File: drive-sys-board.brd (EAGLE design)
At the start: 109.9 x 50.2 mm, 31 parts, among them J2 APP_2POS_CONFIG12V_HORIZ, U1 OKI-78SR-5/1.5-W36HC, U2 MAX232, U3 MAX232, U4 MAX232

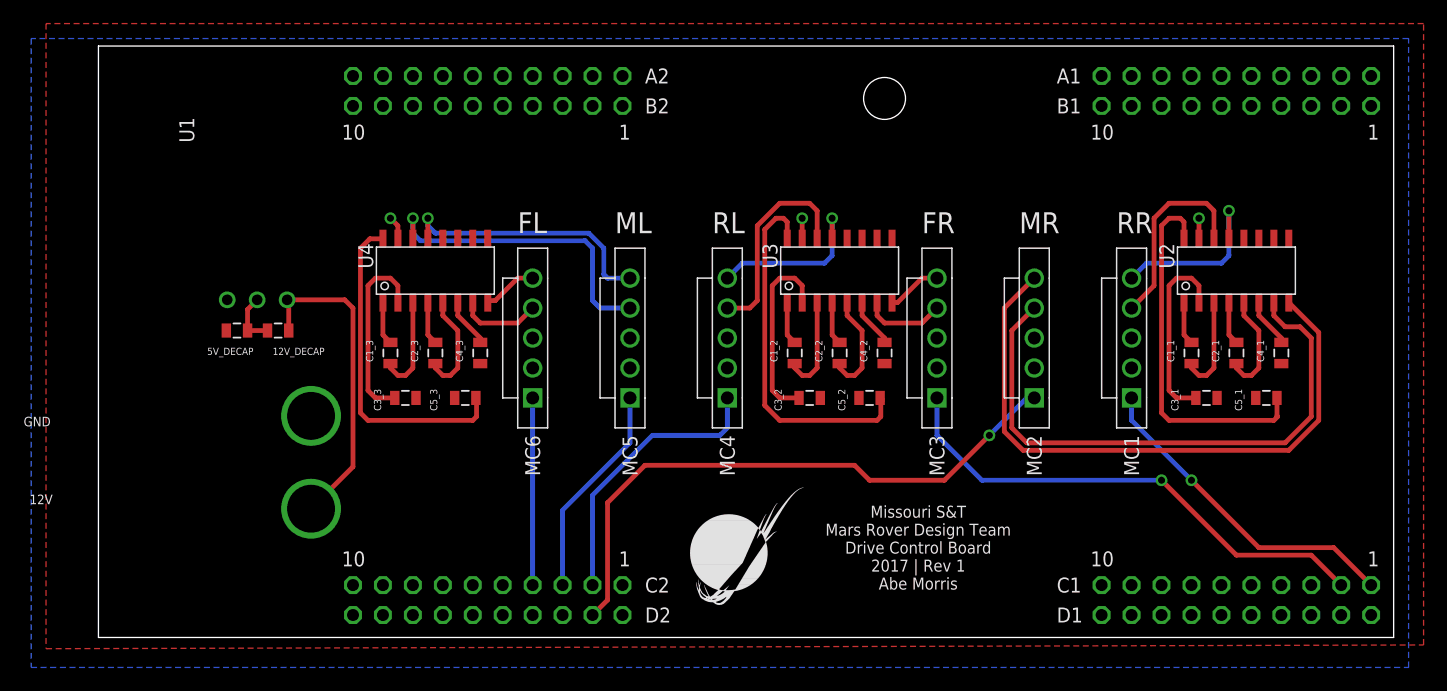
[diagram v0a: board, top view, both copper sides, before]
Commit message: Fixed RS232 chip capacitors
Several capacitors were going to Vcc when they should have been going to
Gnd
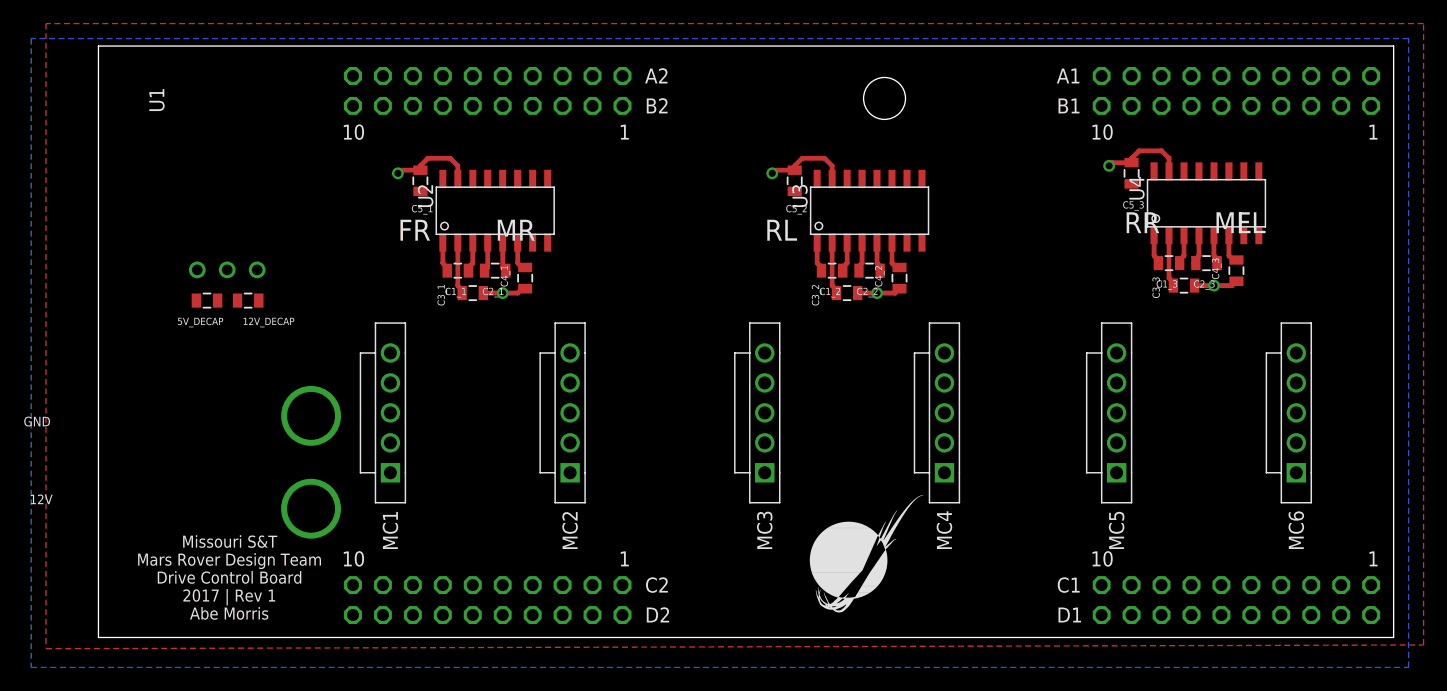
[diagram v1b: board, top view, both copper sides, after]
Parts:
- moved C5_1 74.1 mm to (27.3, 38.7), turned to 270 degrees
- moved C3_3 66.7 mm to (92.1, 29.8)
- moved C1_3 66.5 mm to (90.8, 31.8), turned to 180 degrees
- moved C2_3 65.8 mm to (94.0, 31.8), turned to 180 degrees
- moved U4 65.7 mm to (94.0, 36.8)
- moved MC6 65.1 mm to (101.6, 19.1)
- moved C4_3 64.5 mm to (96.5, 31.1)
- moved C4_1 64.4 mm to (36.2, 30.5)
- moved C2_1 63.3 mm to (33.7, 31.1), turned to 180 degrees
- moved MC1 63.2 mm to (24.8, 19.1)
- moved U2 63.1 mm to (33.7, 36.2)
- moved C3_1 62.9 mm to (31.8, 29.2)
- moved C1_1 62.6 mm to (30.5, 31.1), turned to 180 degrees
- moved C5_3 59.6 mm to (87.6, 39.4), turned to 270 degrees
- moved MC5 41.8 mm to (86.4, 19.1)
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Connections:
- removed net N$10: C5_1.1, U2.16
- removed net N$17: C5_2.1, U3.16
- removed net N$24: C5_3.1, U4.16
- net +5V: now also U2.16, U3.16, U4.16; no longer C3_1.1, C3_2.1, C3_3.1, C4_1.1, C4_2.1, C4_3.1
- net GND: now also C3_1.1, C3_2.1, C3_3.1, C4_1.1, C4_2.1, C4_3.1, C5_1.1, C5_2.1, C5_3.1
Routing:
- net N$34: track 53.5 -> 0.00 mm
- net PWM_2: track 51.0 -> 0.00 mm, vias 1 -> 0
- net N$35: track 49.5 -> 0.00 mm
- net PWM_3: track 42.7 -> 0.00 mm, vias 1 -> 0
- net N$10: track 31.4 -> 0.00 mm
- net N$17: track 31.1 -> 0.00 mm
- net N$24: track 28.1 -> 0.00 mm
- net PWM_1: track 28.0 -> 0.00 mm, vias 1 -> 0
- net N$5: track 27.0 -> 0.00 mm
- net N$26: track 26.7 -> 0.00 mm, vias 1 -> 0
- net PWM_4: track 24.0 -> 0.00 mm
- net N$29: track 22.7 -> 0.00 mm, vias 1 -> 0
- net GND: track 10.1 -> 32.7 mm, vias 3 -> 6
- net PWM_5: track 18.2 -> 0.00 mm
- net N$32: track 17.7 -> 0.00 mm
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
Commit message: Began routing traces
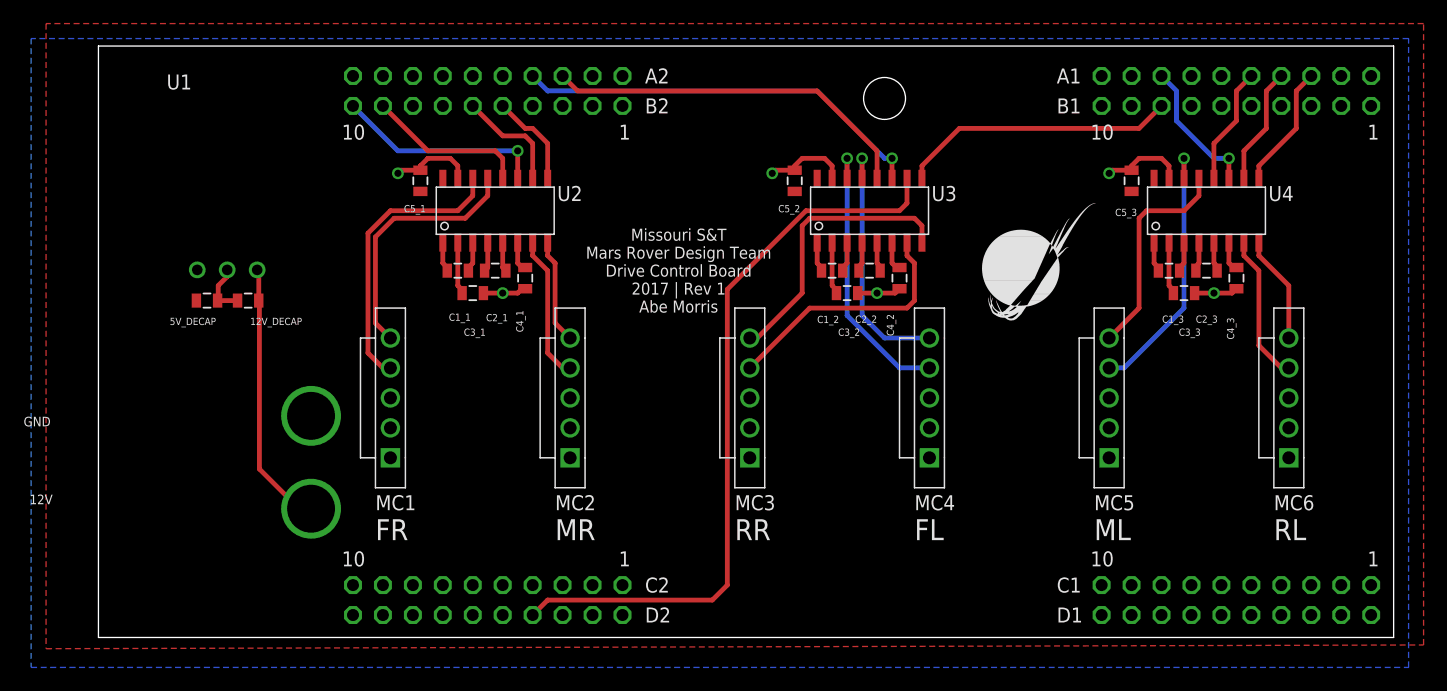
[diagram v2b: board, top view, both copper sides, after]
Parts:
- moved U$2 28.8 mm to (74.9, 26.0)
- moved MC3 1.80 mm to (55.2, 20.3)
- moved MC4 1.80 mm to (70.5, 20.3)
- moved MC5 1.42 mm to (85.7, 20.3)
- moved MC6 1.42 mm to (101.0, 20.3)
- moved MC1 1.27 mm to (24.8, 20.3)
- moved MC2 1.27 mm to (40.0, 20.3)
- moved C1_3 0.64 mm to (90.8, 31.1)
- moved C2_3 0.64 mm to (94.0, 31.1)
- moved C3_3 0.63 mm to (92.1, 29.2)
- moved C4_3 0.63 mm to (96.5, 30.5)
- moved C5_3 0.63 mm to (87.6, 38.7)
- moved U4 0.63 mm to (94.0, 36.2)
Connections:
- new net PWM1: U$1.PF1
- new net PWM2: U$1.PM7
- new net PWM3: U$1.PF2
- new net PWM4: U$1.PK4
- new net PWM5: U$1.PK5
- new net PWM6: U$1.PM0
- net PWM_1: no longer U$1.PF1
- net PWM_2: no longer U$1.PM7
- net PWM_3: no longer U$1.PF2
- net PWM_4: no longer U$1.PK4
- net PWM_5: no longer U$1.PK5
- net PWM_6: no longer U$1.PM0
- net RX_1: now also U$1.PA4; no longer U$1.PA6
- net RX_2: now also U$1.PK0; no longer U$1.PA4
- net RX_3: now also U$1.PP0; no longer U$1.PK0
- net RX_4: now also U$1.PA6; no longer U$1.PC6
- net RX_5: now also U$1.PC6; no longer U$1.PP0
- net TX_1: now also U$1.PA5; no longer U$1.PA7
- net TX_2: now also U$1.PK1; no longer U$1.PA5
- net TX_3: now also U$1.PP1; no longer U$1.PK1
- net TX_4: now also U$1.PA7; no longer U$1.PC7
- net TX_5: now also U$1.PC7; no longer U$1.PP1
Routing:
- net TX_4: track 0.00 -> 63.0 mm
- net TX_3: track 0.00 -> 35.1 mm, vias 0 -> 1
- net RX_3: track 0.00 -> 31.7 mm
- net N$36: track 0.00 -> 24.2 mm
- net N$32: track 0.00 -> 23.9 mm, vias 0 -> 1
- net N$30: track 0.00 -> 23.9 mm
- net RX_4: track 0.00 -> 23.5 mm
- net N$26: track 0.00 -> 22.9 mm, vias 0 -> 1
- net N$5: track 0.00 -> 22.7 mm
- net N$33: track 0.00 -> 21.6 mm, vias 0 -> 1
- net N$31: track 0.00 -> 21.5 mm
- net N$37: track 0.00 -> 21.5 mm
- net N$29: track 0.00 -> 18.5 mm
- net TX_1: track 0.00 -> 17.9 mm, vias 0 -> 1
- net RX_1: track 0.00 -> 13.7 mm
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
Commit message: Updated Max232 and Tiva to Eagle libraries commit 9c171e
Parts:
- U$1: value TIVA-C-CONNECTED -> TIVA-1294; device MRDT-2015-General:TIVA-C-CONNECTED -> MRDT-Microcontrollers:TIVA-C-CONNECTED
- U2, U3, U4: value MAX232 -> MAX232D
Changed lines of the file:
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@@
 <?xml version="1.0" encoding="utf-8"?>
 <!DOCTYPE eagle SYSTEM "eagle.dtd">
-<eagle version="7.7.0">
+<eagle version="7.6.0">
 <drawing>
 <settings>
@@
 </autorouter>
 <elements>
-<element name="U$1" library="MRDT-2015-General" package="TIVA-C-CONNECTED" value="TIVA-C-CONNECTED" x="-15.24" y="-6.985" smashed="yes"/>
+<element name="U$1" library="MRDT-Microcontrollers" package="TIVA-C-CONNECTED" value="TIVA-1294" x="-15.24" y="-6.985" smashed="yes"/>
 <element name="U$2" library="MRDT-2015-General" package="MRDT_LOGO" value="" x="74.93" y="26.035"/>
 <element name="U1" library="MRDT-ICs" package="OKI-78SR_HORIZ" value="OKI-78SR-5/1.5-W36HC" x="13.462" y="31.1785" smashed="yes">
@@
 <attribute name="COLOR2" value="BLACK" x="-10.16" y="6.985" size="1.778" layer="27" display="off"/>
 </element>
-<element name="U2" library="MRDT-ICs" package="SOIC16" value="MAX232" x="33.655" y="36.195" smashed="yes">
+<element name="U2" library="MRDT-ICs" package="SOIC16" value="MAX232D" x="33.655" y="36.195" smashed="yes">
 <attribute name="NAME" x="38.91" y="37.02" size="1.27" layer="25" font="vector"/>
 <attribute name="VALUE" x="30.655" y="31.195" size="1.27" layer="27" font="vector"/>
+<attribute name="OPERATING_VOLTAGE" value="5V" x="33.655" y="36.195" size="1.778" layer="27" display="off"/>
 </element>
 <element name="H2" library="MRDT-Hardware" package="#6_SCREW" value="MOUNTING_HOLE#6" x="66.675" y="45.72"/>
@@
 <attribute name="VALUE" x="25.908" y="39.751" size="0.4064" layer="27" rot="R270"/>
 </element>
-<element name="U3" library="MRDT-ICs" package="SOIC16" value="MAX232" x="65.405" y="36.195" smashed="yes">
+<element name="U3" library="MRDT-ICs" package="SOIC16" value="MAX232D" x="65.405" y="36.195" smashed="yes">
 <attribute name="NAME" x="70.66" y="37.02" size="1.27" layer="25" font="vector"/>
 <attribute name="VALUE" x="62.405" y="31.195" size="1.27" layer="27" font="vector"/>
+<attribute name="OPERATING_VOLTAGE" value="5V" x="65.405" y="36.195" size="1.778" layer="27" display="off"/>
 </element>
 <element name="C1_2" library="SparkFun-Capacitors" package="0805" value="1uF" x="62.23" y="31.115" smashed="yes" rot="R180">
@@
 <attribute name="VALUE" x="57.658" y="39.751" size="0.4064" layer="27" rot="R270"/>
 </element>
-<element name="U4" library="MRDT-ICs" package="SOIC16" value="MAX232" x="93.98" y="36.195" smashed="yes">
+<element name="U4" library="MRDT-ICs" package="SOIC16" value="MAX232D" x="93.98" y="36.195" smashed="yes">
 <attribute name="NAME" x="99.235" y="37.02" size="1.27" layer="25" font="vector"/>
 <attribute name="VALUE" x="90.98" y="31.195" size="1.27" layer="27" font="vector"/>
+<attribute name="OPERATING_VOLTAGE" value="5V" x="93.98" y="36.195" size="1.778" layer="27" display="off"/>
 </element>
 <element name="C1_3" library="SparkFun-Capacitors" package="0805" value="1uF" x="90.805" y="31.115" smashed="yes" rot="R180">
@@
 <signals>
 <signal name="GND">
-<contactref element="U$1" pad="GND_1"/>
-<contactref element="U$1" pad="GND_2"/>
-<contactref element="U$1" pad="GND_3"/>
-<contactref element="U$1" pad="GND_4"/>
+<contactref element="U$1" pad="GND_1" route="any" routetag="G$1.GND"/>
+<contactref element="U$1" pad="GND_2" route="any" routetag="G$1.GND"/>
+<contactref element="U$1" pad="GND_3" route="any" routetag="G$1.GND"/>
+<contactref element="U$1" pad="GND_4" route="any" routetag="G$1.GND"/>
 <polygon width="0.4064" layer="16">
 <vertex x="-5.715" y="50.8"/>
@@
 <vertex x="112.395" y="52.07"/>
 </polygon>
-<contactref element="U$1" pad="+5V_1"/>
-<contactref element="U$1" pad="+5V_2"/>
+<contactref element="U$1" pad="+5V_1" route="any" routetag="G$1.+5V"/>
+<contactref element="U$1" pad="+5V_2" route="any" routetag="G$1.+5V"/>
 <contactref element="5V_DECAP" pad="2"/>
 <contactref element="MC6" pad="2"/>

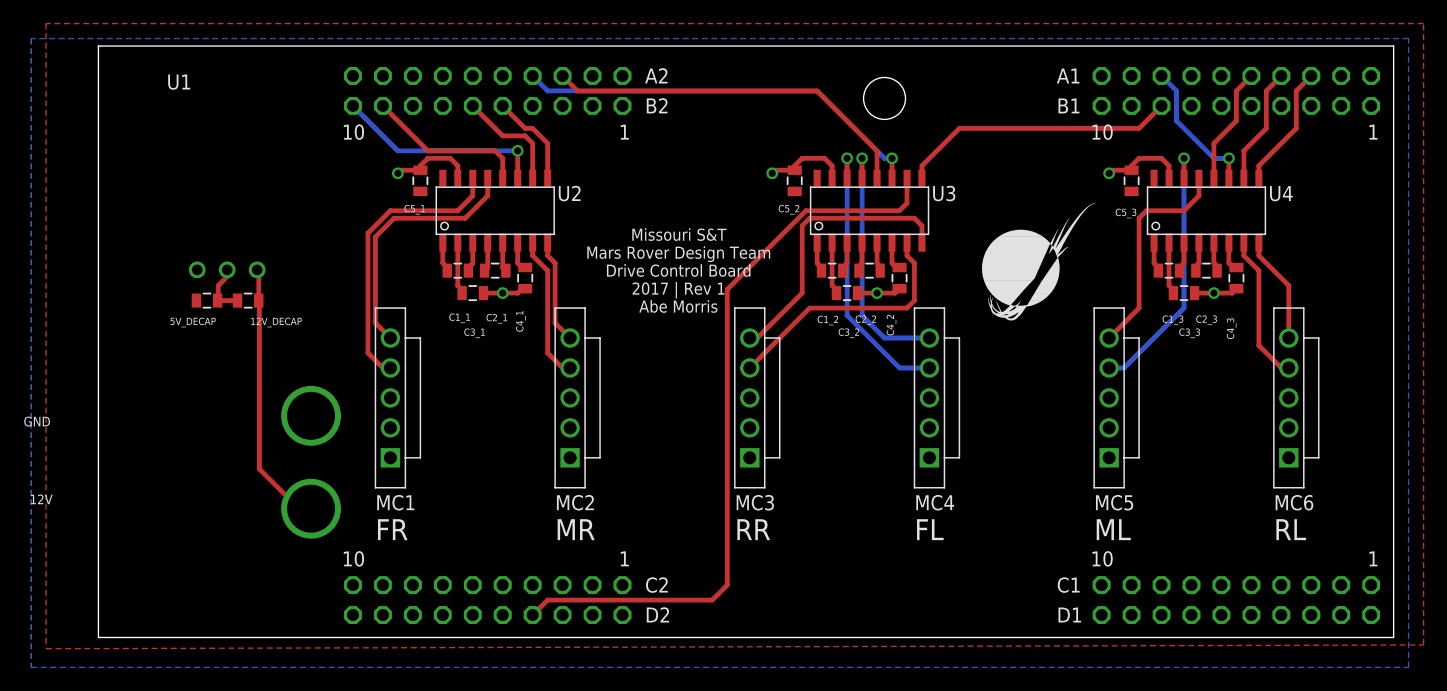
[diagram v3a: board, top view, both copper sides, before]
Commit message: Routed PWM traces and added power indicator led
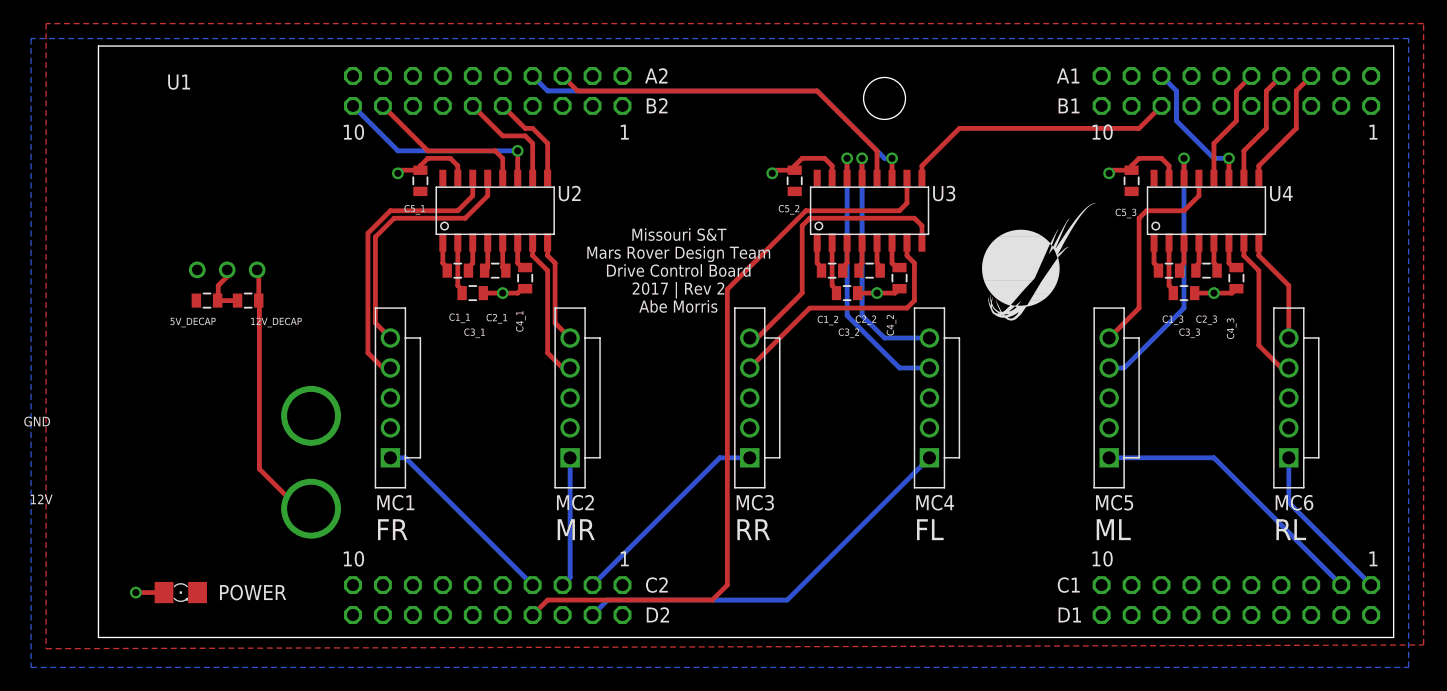
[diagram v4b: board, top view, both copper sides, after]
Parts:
- added POWER: (no value), eagle-ltspice:LED_1206
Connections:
- removed net PWM1: U$1.PF1
- removed net PWM2: U$1.PM7
- removed net PWM3: U$1.PF2
- removed net PWM4: U$1.PK4
- removed net PWM5: U$1.PK5
- removed net PWM6: U$1.PM0
- net +5V: now also POWER.C
- net GND: now also POWER.A
- net PWM_1: now also U$1.PM0
- net PWM_2: now also U$1.PK5
- net PWM_3: now also U$1.PK4
- net PWM_4: now also U$1.PM7
- net PWM_5: now also U$1.PF2
- net PWM_6: now also U$1.PF1
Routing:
- net PWM_4: track 0.00 -> 34.1 mm
- net PWM_5: track 0.00 -> 24.2 mm
- net PWM_3: track 0.00 -> 17.8 mm
- net PWM_1: track 0.00 -> 16.5 mm
- net PWM_6: track 0.00 -> 13.7 mm
- net PWM_2: track 0.00 -> 11.1 mm
- net GND: track 37.3 -> 39.7 mm, vias 6 -> 7
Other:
- board text added: "Missouri S&T Mars Rover Design Team Drive Control Board 2017 | Rev 2 Abe Morris"
- board text removed: "Missouri S&T Mars Rover Design Team Drive Control Board 2017 | Rev 1 Abe Morris"
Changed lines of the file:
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@@
 Mars Rover Design Team
 Drive Control Board
-2017 | Rev 1
+2017 | Rev 2
 Abe Morris</text>
 <dimension x1="0" y1="0" x2="109.22" y2="0" x3="54.61" y3="-12.065" textsize="1.778" layer="47" dtype="horizontal" unit="inch" precision="6" visible="yes"/>
@@
 <attribute name="VALUE" x="13.716" y="29.972" size="0.4064" layer="27" rot="R180"/>
 </element>
+<element name="POWER" library="eagle-ltspice" package="LED_1206" value="" x="6.985" y="3.81" smashed="yes">
+<attribute name="SPICETYPE" value="diode" x="6.985" y="3.81" size="1.778" layer="27" display="off"/>
+<attribute name="SPICEPREFIX" value="D" x="6.985" y="3.81" size="1.778" layer="27" display="off"/>
+<attribute name="SPICEMODEL" value="NONE" x="6.985" y="3.81" size="1.778" layer="27" display="off"/>
+<attribute name="NAME" x="10.16" y="3.175" size="1.27" layer="25"/>
+<attribute name="VALUE" x="5.715" y="1.27" size="1.27" layer="27"/>
+</element>
 </elements>
 <signals>
@@
 <wire x1="10.16" y1="29.845" x2="10.922" y2="30.607" width="0.4064" layer="1"/>
 <wire x1="10.922" y1="30.607" x2="10.922" y2="31.1785" width="0.4064" layer="1"/>
+<contactref element="POWER" pad="A"/>
+<via x="3.175" y="3.81" extent="1-16" drill="0.6" shape="square"/>
+<wire x1="5.563" y1="3.81" x2="3.175" y2="3.81" width="0.4064" layer="1"/>
 </signal>
 <signal name="+5V">
@@
 <contactref element="C5_2" pad="2"/>
 <contactref element="C5_3" pad="2"/>
+<contactref element="POWER" pad="C"/>
 </signal>
 <signal name="PWM_6">
 <contactref element="MC6" pad="1"/>
+<contactref element="U$1" pad="PF1"/>
+<wire x1="100.965" y1="15.24" x2="100.965" y2="11.43" width="0.4064" layer="16"/>
+<wire x1="100.965" y1="11.43" x2="107.95" y2="4.445" width="0.4064" layer="16"/>
 </signal>
 <signal name="RX_1">
@@
 <signal name="PWM_1">
 <contactref element="MC1" pad="1"/>
+<contactref element="U$1" pad="PM0"/>
+<wire x1="24.765" y1="15.24" x2="26.035" y2="15.24" width="0.4064" layer="16"/>
+<wire x1="26.035" y1="15.24" x2="36.83" y2="4.445" width="0.4064" layer="16"/>
 </signal>
 <signal name="PWM_2">
 <contactref element="MC2" pad="1"/>
+<contactref element="U$1" pad="PK5"/>
+<wire x1="40.005" y1="15.24" x2="40.005" y2="5.08" width="0.4064" layer="16"/>
+<wire x1="40.005" y1="5.08" x2="39.37" y2="4.445" width="0.4064" layer="16"/>
 </signal>
 <signal name="RX_2">
@@
 <signal name="PWM_3">
 <contactref element="MC3" pad="1"/>
+<contactref element="U$1" pad="PK4"/>
+<wire x1="55.245" y1="15.24" x2="52.705" y2="15.24" width="0.4064" layer="16"/>
+<wire x1="52.705" y1="15.24" x2="41.91" y2="4.445" width="0.4064" layer="16"/>
 </signal>
 <signal name="RX_3">
@@
 <signal name="PWM_4">
 <contactref element="MC4" pad="1"/>
+<contactref element="U$1" pad="PM7"/>
+<wire x1="70.485" y1="15.24" x2="58.42" y2="3.175" width="0.4064" layer="16"/>
+<wire x1="58.42" y1="3.175" x2="43.18" y2="3.175" width="0.4064" layer="16"/>
+<wire x1="43.18" y1="3.175" x2="41.91" y2="1.905" width="0.4064" layer="16"/>
 </signal>
 <signal name="RX_4">
@@
 <signal name="PWM_5">
 <contactref element="MC5" pad="1"/>
+<contactref element="U$1" pad="PF2"/>
+<wire x1="85.725" y1="15.24" x2="94.615" y2="15.24" width="0.4064" layer="16"/>
+<wire x1="94.615" y1="15.24" x2="105.41" y2="4.445" width="0.4064" layer="16"/>
 </signal>
 <signal name="RX_5">
@@
 <wire x1="35.93" y1="31.38" x2="36.195" y2="31.38" width="0.4064" layer="1"/>
 </signal>
-<signal name="PWM1">
-<contactref element="U$1" pad="PF1"/>
-</signal>
-<signal name="PWM3">
-<contactref element="U$1" pad="PF2"/>
-</signal>
-<signal name="PWM4">
-<contactref element="U$1" pad="PK4"/>
-</signal>
-<signal name="PWM5">
-<contactref element="U$1" pad="PK5"/>
-</signal>
-<signal name="PWM2">
-<contactref element="U$1" pad="PM7"/>
-</signal>
-<signal name="PWM6">
-<contactref element="U$1" pad="PM0"/>
-</signal>
 </signals>
